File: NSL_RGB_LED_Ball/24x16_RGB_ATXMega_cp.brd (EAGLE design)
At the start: 46.4 x 123.7 mm, 109 parts, among them IC2 TLC5947XLP, IC3 TLC5947XLP, IC4 TLC5947XLP, IC5 MCP73123, IC6 BLUETOOTH-RN41", IC7 MMA7455L, IC8 OPA344, Q1 BSH201, X1 NX3225GA XC1972CT-ND

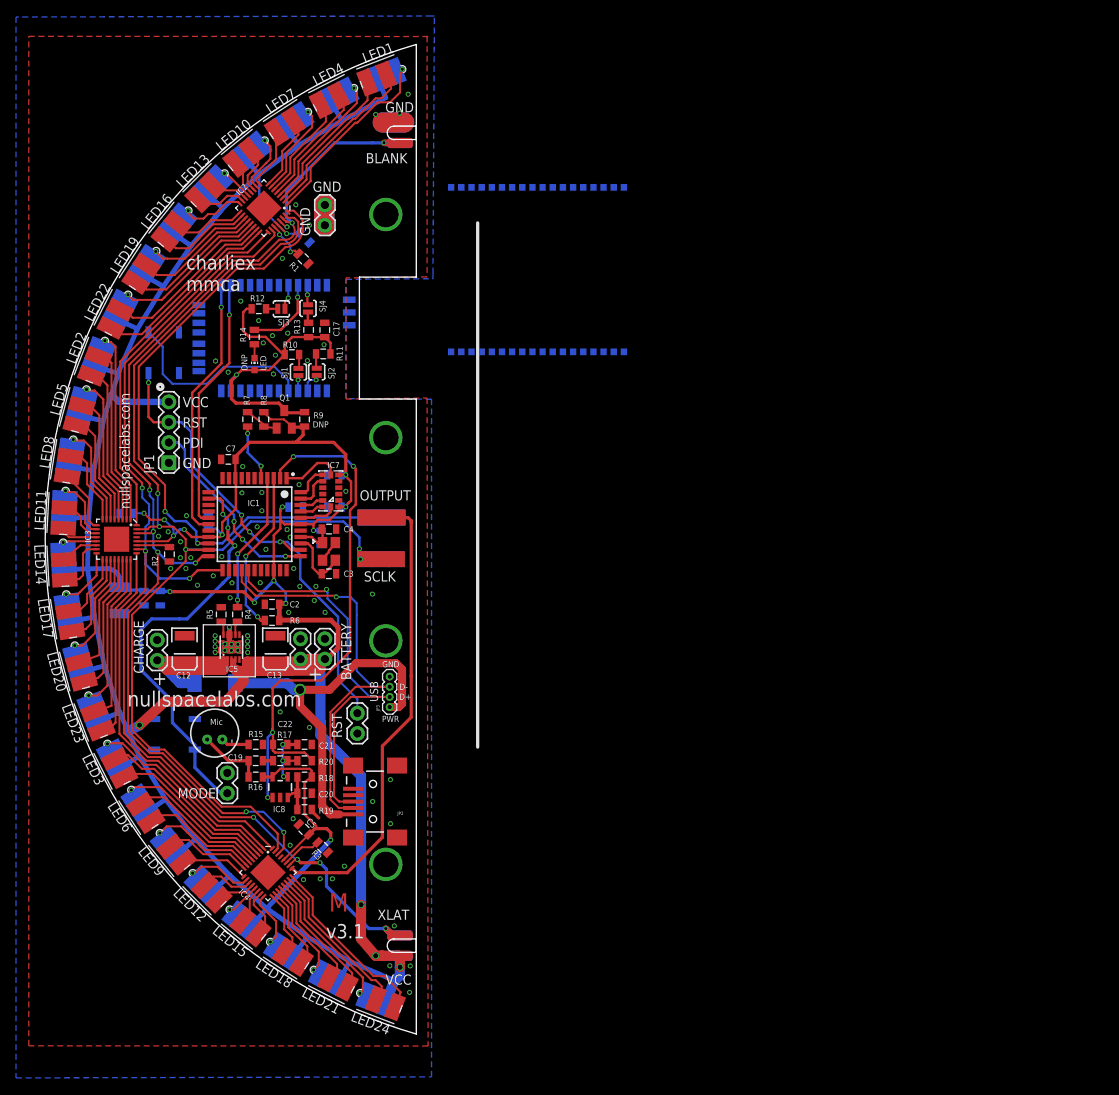
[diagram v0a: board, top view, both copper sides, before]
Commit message: 
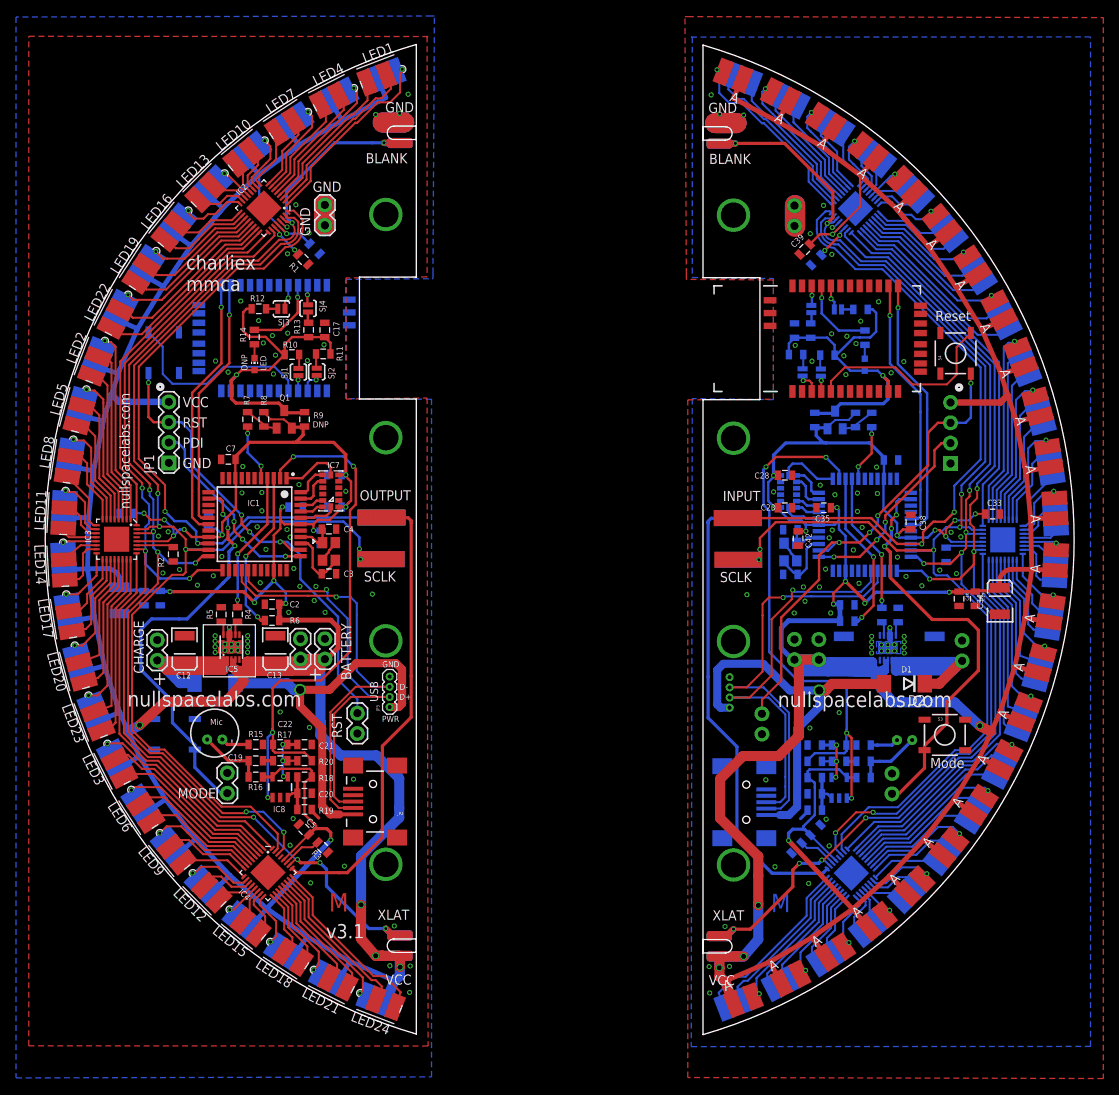
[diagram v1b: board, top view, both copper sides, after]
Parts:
- removed U$5: ZG2100MC, zg2100-mrf24wb0ma:ZG2100MC
- added BATTERY2, BATTERY3, CHARGE1, GND1: (no value), SparkFun:1X02
- added C23, C24, C29, C33, C35, C36, C38, C39: .1uF, slice_noshift:0805
- added C25, C26: 4.7uF, slice_noshift:EIA3528
- added C27, C37: .1uF, SparkFun:0805
- added C28, C42: 0.1uF, SparkFun:0805
- added C30: 4.7uF, SparkFun:0805
- added C31: 1uF, SparkFun:0805
- added C32: 12pF, SparkFun:0805
- added C34: 47uF, slice_noshift:EIA3528
- added C40: 10uF, 24x16_RGB:0805
- added C41: 1uF, 24x16_RGB:0805
- added C43, C44: 10pF, SparkFun:0805
- added D2: SSB44-E3/52T, diode:DO214AA
- added IC10: MCP73123, 24x16_RGB:DFN10_3X3
- added IC11: BLUETOOTH-RN41", NSL_Mini_Quad:RN41
- added IC12, IC13, IC9: TLC5947XLP, slice_noshift:QFN32_XLP
- added IC14: MMA7455L, MMA7455Lbreakoutboard-v1a:LGA-14
- added IC15: OPA344, SparkFun:SOT23-5
- added IC16: (no value), Outline:NONOLITH_TQFP-44
- added JP4: (no value), SparkFun-Connectors:1X04
- added JP5: USBSMD, SparkFun-Connectors:USB-MINIB
- added JP6: (no value), SparkFun-Connectors:1X04-1.27MM
- added LED25, LED26, LED27, LED28, LED29, LED30, LED31, LED32, LED33, LED34, LED35, LED36, LED37, LED38, LED39, LED40, LED41, LED42, LED43, LED44, LED45, LED46, LED47, LED48: GM1WA55311A5MM_RGB_EDGE, 24x16_RGB:LED5MM_RGB_EDGE
- added LED49: (no value), led:CHIP-LED0603
- added MIC2: MIC6MM, slice_noshift:MIC-6MM
- added MODE1, RST1: (no value), 24x16_RGB:1X02
- added Q2: BSH201, transistor-small-signal:SOT23
- added R21, R29, R30: 20K, 24x16_RGB:0805
- added R22, R23: 1K, slice_noshift:0805
- added R24: 220, SparkFun:0805
- added R25, R26, R27, R28: 1k, SparkFun:0805
- added R31: 2.2k, SparkFun:0805
- added R32, R33, R34, R37, R38: 10k, SparkFun:0805
- added R35: 1M, SparkFun:0805
- added R36: 220K, slice_noshift:0805
- added R39: 0ohm DNP, SparkFun:0805
- added R40: 4.7k, SparkFun:0805
- added S3, S4: (no value), SparkFun:TACTILE_SWITCH_SMD
- added SJ5, SJ6, SJ7, SJ8: SOLDERJUMPERNO, SparkFun:SJ_2S-NO
- added SLOT3, SLOT4: SLOT, slice:SLOT
- added TP13, TP14, TP15, TP16, TP17, TP18, TP19, TP20, TP21, TP22, TP23, TP24: TPTP20SQ, testpad:TP20SQ
- added X2: NX3225GA XC1972CT-ND, M6-RF315:NX3225GA
- moved C11 1.91 mm to (-30.5, 36.3)
- moved R2 0.48 mm to (-48.2, -1.88)
- moved R1 0.08 mm to (-31.9, 35.0)
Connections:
- new net !CS1: IC14.7, IC16.1
- new net BATTSENSE1: IC16.3, R36.2
- new net BLANK1: IC12.30, IC13.30, IC16.22, IC9.30, SLOT4.P$1, SLOT4.P$3
- new net BT_PWR1: IC16.5, R38.2
- new net BT_RST1: IC11.5, S4.4
- new net BUTTON1: IC16.13, MODE1.2, S3.3
- new net CHARGE1: C25.A, CHARGE1.2, D2.C, IC10.1, IC10.2
- new net COL100: IC12.4, LED34.B
- new net COL101: IC12.5, LED34.G
- new net COL102: IC12.6, LED34.R
- new net COL103: IC12.7, LED35.B
- new net COL104: IC12.8, LED35.G
- new net COL105: IC12.9, LED35.R
- new net COL106: IC12.10, LED36.B
- new net COL107: IC12.11, LED36.G
- new net COL108: IC12.12, LED36.R
- new net COL109: IC12.13, LED37.B
- new net COL110: IC12.14, LED37.G
- new net COL111: IC12.15, LED37.R
- new net COL112: IC12.16, LED38.B
- new net COL113: IC12.17, LED38.G
- new net COL114: IC12.18, LED38.R
- new net COL115: IC12.19, LED39.B
- new net COL116: IC12.20, LED39.G
- new net COL117: IC12.21, LED39.R
- new net COL118: IC12.22, LED40.B
- new net COL119: IC12.23, LED40.G
- new net COL120: IC12.24, LED40.R
- new net COL121: IC13.1, LED41.B
- new net COL122: IC13.2, LED41.G
- new net COL123: IC13.4, LED42.B
- new net COL124: IC13.3, LED41.R
- new net COL125: IC13.5, LED42.G
- new net COL126: IC13.6, LED42.R
- new net COL127: IC13.7, LED43.B
- new net COL128: IC13.8, LED43.G
- new net COL129: IC13.9, LED43.R
- new net COL130: IC13.10, LED44.B
- new net COL131: IC13.11, LED44.G
- new net COL132: IC13.12, LED44.R
- new net COL133: IC13.13, LED45.B
- new net COL134: IC13.14, LED45.G
- new net COL135: IC13.15, LED45.R
- new net COL136: IC13.16, LED46.B
- new net COL137: IC13.17, LED46.G
- new net COL138: IC13.18, LED46.R
- new net COL139: IC13.19, LED47.B
- new net COL140: IC13.20, LED47.G
- new net COL141: IC13.21, LED47.R
- new net COL142: IC13.22, LED48.B
- new net COL143: IC13.23, LED48.G
- new net COL144: IC13.24, LED48.R
- new net COL73: IC9.2, LED25.G
- new net COL74: IC9.4, LED26.B
- new net COL75: IC9.5, LED26.G
- new net COL76: IC9.7, LED27.B
- new net COL77: IC9.8, LED27.G
- new net COL78: IC9.10, LED28.B
- new net COL79: IC9.11, LED28.G
- new net COL80: IC9.13, LED29.B
- new net COL81: IC9.14, LED29.G
- new net COL82: IC9.17, LED30.G
- new net COL83: IC9.19, LED31.B
- new net COL84: IC9.20, LED31.G
- new net COL85: IC9.23, LED32.G
- new net COL86: IC9.22, LED32.B
- new net COL87: IC9.16, LED30.B
- new net COL88: IC9.1, LED25.B
- new net COL89: IC9.3, LED25.R
- new net COL90: IC9.6, LED26.R
- new net COL91: IC9.9, LED27.R
- new net COL92: IC9.12, LED28.R
- new net COL93: IC9.15, LED29.R
- new net COL94: IC9.18, LED30.R
- new net COL95: IC9.21, LED31.R
- new net COL96: IC9.24, LED32.R
- new net COL97: IC12.3, LED33.R
- new net COL98: IC12.1, LED33.B
- new net COL99: IC12.2, LED33.G
- new net D+1: IC16.27, JP5.D+, JP6.2
- new net D-1: IC16.26, JP5.D-, JP6.3
- new net DAT1: IC16.34, JP4.2
- new net DGND1: X2.2, X2.4
- new net GND1: BATTERY2.1, BATTERY3.1, C23.2, C24.2, C25.C, C26.C, C27.2, C28.1, C29.2, C31.1, C33.2, C34.C, C35.2, C36.2, C37.2, C38.2, C39.2, C40.2, C41.2, C42.2, C43.1, C44.1, CHARGE1.1, GND1.1, GND1.2, IC10.8, IC10.9, IC10.EXP, IC11.1, IC11.12, IC11.25, IC11.27, IC11.28, IC11.29, IC12.29, IC13.29, IC14.10, IC14.11, IC14.2, IC14.3, IC14.4, IC14.5, IC15.2, IC16.18, IC16.30, IC16.38, IC16.8, IC9.29, JP4.1, JP5.GND, JP6.4, MODE1.1, R21.1, R22.1, R29.1, R30.1, R34.2, R40.1, RST1.1, S3.1, S3.2, S4.1, S4.2, SLOT4.P$2, SLOT4.P$4
- new net HOLE1: IC9.27, R21.2
- new net INT1: IC14.9, IC16.43
- new net INT1/DRDY1: IC14.8, IC16.44
- new net MIC1: C32.1, IC15.1, IC16.2, R35.2
- new net N$22: IC10.7, R23.2
- new net N$25: LED49.C, R24.2
- new net N$26: R27.1, SJ7.2
- new net N$27: R25.1, SJ5.2
- new net N$28: R26.1, SJ6.2
- new net N$29: R28.1, SJ8.2
- new net N$30: IC12.27, R29.2
- new net N$31: IC12.32, IC9.25
- new net N$32: IC13.27, R30.2
- new net N$39: C30.2, R33.2
- new net N$40: C30.1, MIC2.1, R31.1
- new net N$41: C31.2, IC15.3, R32.1, R34.1
- new net N$42: C32.2, C37.1, IC15.4, R33.1, R35.1
- new net N$43: Q2.1, R37.1, R38.1
- new net N$44: IC12.25, IC13.32
- new net N$45: MIC2.2, R40.2
- new net N$46: C44.2, IC16.36, X2.3
- new net N$47: C43.2, IC16.37, X2.1
- new net N$48: D2.A, JP5.VBUS, JP6.1
- new net N$8: IC10.10, R22.2
- new net PIO1: IC11.21, R24.1
- new net PIO10: IC11.20, SJ7.1
- new net PIO2: IC11.22, SJ8.1
- new net PIO8: IC11.3, SJ6.1
- new net PIO9: IC11.4, SJ5.1
- new net RST1: IC16.35, JP4.3, RST1.2, S4.3
- new net RX1: IC11.14, IC16.16
- new net SCL/SPC1: IC14.13, IC16.41
- new net SCLK1: IC12.31, IC13.31, IC16.21, IC9.31, TP15.TP, TP16.TP, TP19.TP, TP20.TP, TP22.TP, TP24.TP
- new net SDA/SDI/SDO1: IC14.12, IC16.42
- new net SDO1: IC14.14, IC16.40
- new net SIN1: IC16.20, IC9.32, TP17.TP, TP18.TP, TP23.TP
- new net SOUT1: IC13.25, TP13.TP, TP14.TP, TP21.TP
- new net STAT1: IC16.4, R23.1
- new net TX1: IC11.13, IC16.17
- new net VCC1: BATTERY2.2, BATTERY3.2, C23.1, C24.1, C26.A, C28.2, C29.1, C33.1, C34.A, C35.1, C36.1, C38.1, C39.1, C40.1, C41.1, C42.1, IC10.3, IC10.4, IC12.28, IC13.28, IC14.1, IC14.6, IC15.5, IC16.19, IC16.31, IC16.39, IC16.9, IC9.28, JP4.4, LED25.A, LED26.A, LED27.A, LED28.A, LED29.A, LED30.A, LED31.A, LED32.A, LED33.A, LED34.A, LED35.A, LED36.A, LED37.A, LED38.A, LED39.A, LED40.A, LED41.A, LED42.A, LED43.A, LED44.A, LED45.A, LED46.A, LED47.A, LED48.A, Q2.2, R31.2, R32.2, R36.1, R37.2, R39.2, SLOT3.P$1, SLOT3.P$3
- new net VDD1: C27.1, IC11.11, LED49.A, Q2.3, R25.2, R26.2, R27.2, R28.2, R39.1
- new net XLAT1: IC12.26, IC13.26, IC16.23, IC9.26, SLOT3.P$2, SLOT3.P$4
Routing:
- net VCC1: track 0.00 -> 551.4 mm, vias 0 -> 19
- net SCLK1: track 0.00 -> 161.1 mm, vias 0 -> 5
- net BLANK1: track 0.00 -> 139.0 mm, vias 0 -> 8
- net XLAT1: track 0.00 -> 138.6 mm, vias 0 -> 7
- net SIN1: track 0.00 -> 86.6 mm, vias 0 -> 2
- net MIC1: track 0.00 -> 69.3 mm, vias 0 -> 4
- net SOUT1: track 0.00 -> 63.6 mm
- net RST1: track 0.00 -> 60.4 mm, vias 0 -> 4
- net D-1: track 0.00 -> 53.3 mm, vias 0 -> 1
- net BUTTON1: track 0.00 -> 51.6 mm, vias 0 -> 3
- net D+1: track 0.00 -> 50.7 mm, vias 0 -> 1
- net N$48: track 0.00 -> 48.9 mm, vias 0 -> 1
- net N$44: track 0.00 -> 48.5 mm
- net N$31: track 0.00 -> 46.5 mm
- net VDD1: track 0.00 -> 42.2 mm, vias 0 -> 1
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- added copper zone on layer 1, net GND1
- added copper zone on layer 16, net GND1
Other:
- board size 46.4 x 123.7 mm -> 128.6 x 123.8 mm
